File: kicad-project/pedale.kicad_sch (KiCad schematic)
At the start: 10 parts

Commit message: modificari dupa sugestii
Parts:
- removed U9: ~, Connector_PinHeader_2.54mm:PinHeader_1x01_P2.54mm_Vertical, symbol pedale-lib:Conn_J23
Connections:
- net 12V: now also J13.2 (VBAT)
- net GND: no longer J1.11 (GND), J13.14 (GND), J2.7 (GND), J4.10 (GND)
- no-connect marks 104 -> 107

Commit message: modificari 2
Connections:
- net 12V: now also J13.1 (VBAT); no longer J13.2 (VBAT)
- net GND: now also J13.11 (GND); no longer J13.12 (GND)

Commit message: viorel approved
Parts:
- added D1: SS32, Diode_SMD:D_SMA, symbol Diode:SS32
- U1, U8: footprint Connector_PinSocket_2.00mm:PinSocket_1x02_P2.00mm_Horizontal -> Connector_JST:JST_PH_B2B-PH-K_1x02_P2.00mm_Vertical
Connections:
- net 12V: now also D1.1 (K)
- net GND: now also D1.2 (A)
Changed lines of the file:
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@@
+		(color 0 0 0 0)
+	)
+	(junction
+		(at 87.63 50.8)
+		(diameter 0)
+		(color 0 0 0 0)
+	)
+	(junction
+		(at 95.25 48.26)
+		(diameter 0)
 		(color 0 0 0 0)
 	)
@@
 	(wire
 		(pts
-			(xy 87.63 48.26) (xy 87.63 53.34)
+			(xy 87.63 48.26) (xy 87.63 50.8)
 		)
 		(stroke
@@
 	(wire
 		(pts
-			(xy 144.78 45.72) (xy 163.83 45.72)
+			(xy 87.63 50.8) (xy 87.63 53.34)
 		)
 		(stroke
@@
 	(wire
 		(pts
+			(xy 144.78 45.72) (xy 163.83 45.72)
+		)
+		(stroke
+			(width 0)
+			(type default)
+		)
+	)
+	(wire
+		(pts
+			(xy 95.25 48.26) (xy 90.17 48.26)
+		)
+		(stroke
+			(width 0)
+			(type default)
+		)
+	)
+	(wire
+		(pts
 			(xy 76.2 53.34) (xy 87.63 53.34)
+		)
+		(stroke
+			(width 0)
+			(type default)
+		)
+	)
+	(wire
+		(pts
+			(xy 100.33 48.26) (xy 95.25 48.26)
+		)
+		(stroke
+			(width 0)
+			(type default)
+		)
+	)
+	(wire
+		(pts
+			(xy 95.25 48.26) (xy 95.25 50.8)
 		)
 		(stroke
@@
 			)
 		)
-		(property "Footprint" "Connector_PinSocket_2.00mm:PinSocket_1x02_P2.00mm_Horizontal"
+		(property "Footprint" "Connector_JST:JST_PH_B2B-PH-K_1x02_P2.00mm_Vertical"
 			(at 171.45 44.45 0)
 			(effects
@@
 	)
 	(symbol
+		(lib_id "Diode:SS32")
+		(at 91.44 50.8 0)
+		(unit 1)
+		(exclude_from_sim no)
+		(in_bom yes)
+		(on_board yes)
+		(dnp no)
+		(fields_autoplaced yes)
+		(property "Reference" "D1"
+			(at 91.1225 44.45 0)
+			(effects
+				(font
+					(size 1.27 1.27)
+				)
+			)
+		)
+		(property "Value" "SS32"
+			(at 91.1225 46.99 0)
+			(effects
+				(font
+					(size 1.27 1.27)
+				)
+			)
+		)
+		(property "Footprint" "Diode_SMD:D_SMA"
+			(at 91.44 55.245 0)
+			(effects
+				(font
+					(size 1.27 1.27)
+				)
+				(hide yes)
+			)
+		)
+		(property "Datasheet" "https://www.vishay.com/docs/88751/ss32.pdf"
+			(at 91.44 50.8 0)
+			(effects
+				(font
+					(size 1.27 1.27)
+				)
+				(hide yes)
+			)
+		)
+		(property "Description" "20V 3A Schottky Diode, SMA"
+			(at 91.44 50.8 0)
+			(effects
+				(font
+					(size 1.27 1.27)
+				)
+				(hide yes)
+			)
+		)
+		(pin "1"
+		)
+		(pin "2"
+		)
+		(instances
+			(project ""
+				(path "/62a57360-3e57-41ad-98c3-de6f40bd380e"
+					(reference "D1")
+					(unit 1)
+				)
+			)
+		)
+	)
+	(symbol
 		(lib_id "pedale-lib:Conn_J15")
 		(at 241.3 101.6 0)
@@
 			)
 		)
-		(property "Footprint" "Connector_PinSocket_2.00mm:PinSocket_1x02_P2.00mm_Horizontal"
+		(property "Footprint" "Connector_JST:JST_PH_B2B-PH-K_1x02_P2.00mm_Vertical"
 			(at 88.9 43.18 0)
 			(effects
@@
 	(symbol
 		(lib_id "power:GND")
-		(at 90.17 48.26 0)
+		(at 100.33 48.26 90)
 		(unit 1)
 		(exclude_from_sim no)
@@
 		(fields_autoplaced yes)
 		(property "Reference" "#PWR01"
-			(at 90.17 54.61 0)
+			(at 106.68 48.26 0)
 			(effects
 				(font
@@
 		)
 		(property "Value" "GND"
-			(at 90.17 53.34 0)
+			(at 105.41 48.26 0)
 			(effects
 				(font
@@
 		)
 		(property "Footprint" ""
-			(at 90.17 48.26 0)
+			(at 100.33 48.26 0)
 			(effects
 				(font
@@
 		)
 		(property "Datasheet" ""
-			(at 90.17 48.26 0)
+			(at 100.33 48.26 0)
 			(effects
 				(font
@@
 		)
 		(property "Description" "Power symbol creates a global label with name \"GND\" , ground"
-			(at 90.17 48.26 0)
-			(effects
-				(font
+			(at 100.33 48.26 0)
+			(effects
+				(font

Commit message: corectat footprint dioda
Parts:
- D1: footprint Diode_SMD:D_SMA -> Diode_SMD:D_SMB
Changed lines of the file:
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@@
 			)
 		)
-		(property "Footprint" "Diode_SMD:D_SMA"
+		(property "Footprint" "Diode_SMD:D_SMB"
 			(at 91.44 55.245 0)
 			(effects

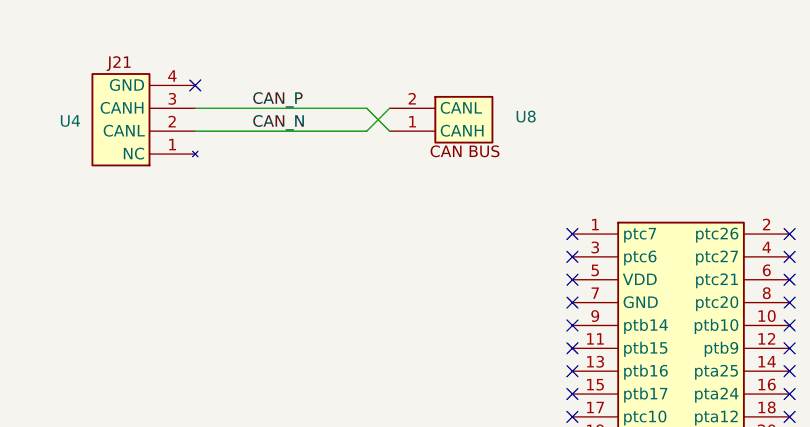
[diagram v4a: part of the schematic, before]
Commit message: CAN_IN & CAN_OUT - added
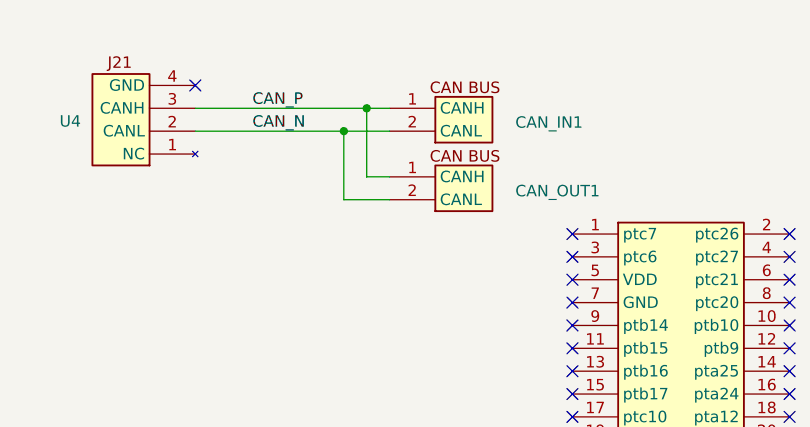
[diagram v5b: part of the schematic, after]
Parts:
- added CAN_OUT1: (no value), Connector_JST:JST_PH_B2B-PH-K_1x02_P2.00mm_Vertical, symbol pedale-lib:Conn_CAN
- CAN_IN1: renamed from U8; value ~ -> (none)
- J1, J13, J14, J2, J3, J4, U1, U4: value ~ -> (none)
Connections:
- net CAN_N: now also CAN_OUT1.2 (CANL)
- net CAN_P: now also CAN_OUT1.1 (CANH)
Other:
- moved on the sheet: CAN_IN1
